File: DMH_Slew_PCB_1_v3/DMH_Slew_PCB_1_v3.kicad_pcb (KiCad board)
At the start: 2 copper layers, 48 x 175 mm, 147 parts, among them J0 Conn_01x01, J1 TS_Jack_6.35mm_Sw, J10 TS_Jack_6.35mm_Sw, J100 IDC_02x08, J2 TS_Jack_6.35mm_Sw, J200 IDC_02x05, J3 TS_Jack_6.35mm_Sw, J4 TS_Jack_6.35mm_Sw, J5 TS_Jack_6.35mm_Sw, J50 Conn_01x08_PinHeader, J51 Conn_01x08_PinHeader, J6 TS_Jack_6.35mm_Sw, J60 Conn_01x08_PinHeader, J61 Conn_01x08_PinHeader, J7 TS_Jack_6.35mm_Sw, J8 TS_Jack_6.35mm_Sw, J9 TS_Jack_6.35mm_Sw, Q1 BC548, Q10 BC558, Q11 BC548, Q12 BC548, Q2 BC548, Q3 BC558, Q4 BC558, Q5 BC548, Q6 BC548, Q7 BC548, Q8 BC548, Q9 BC558, U1 TL074, U10 LM4040LP-10, U11 LM4040LP-10, U2 TL074, U3 TL074, U4 TL074

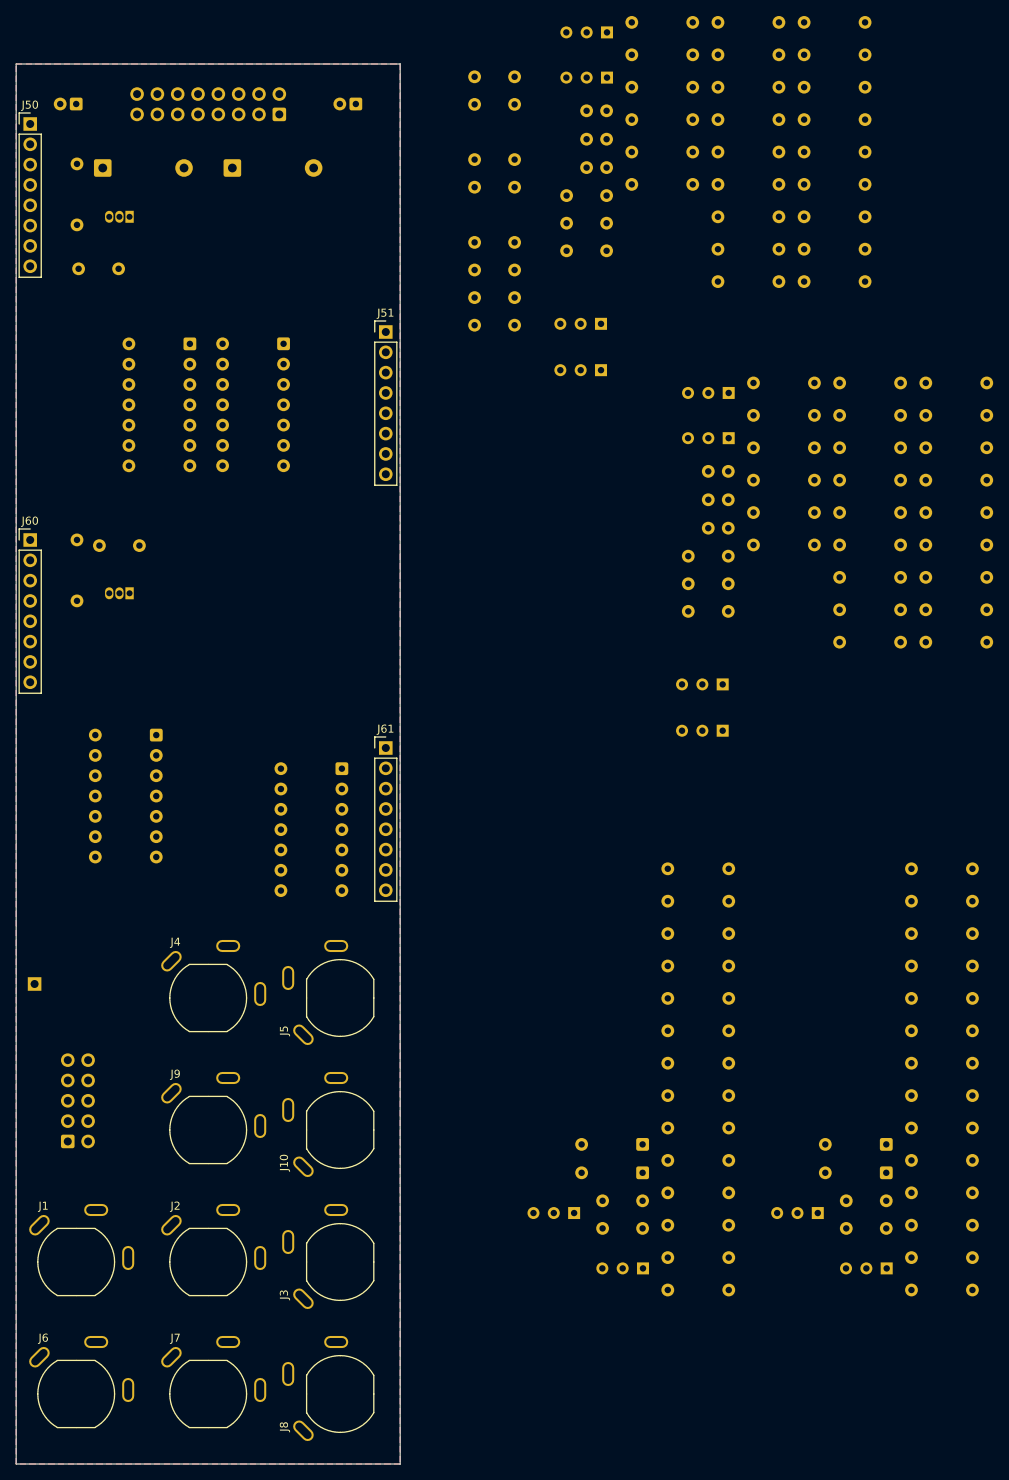
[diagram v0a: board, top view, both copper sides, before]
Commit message: Relinked PCB1 and 2 with new v3 schematics
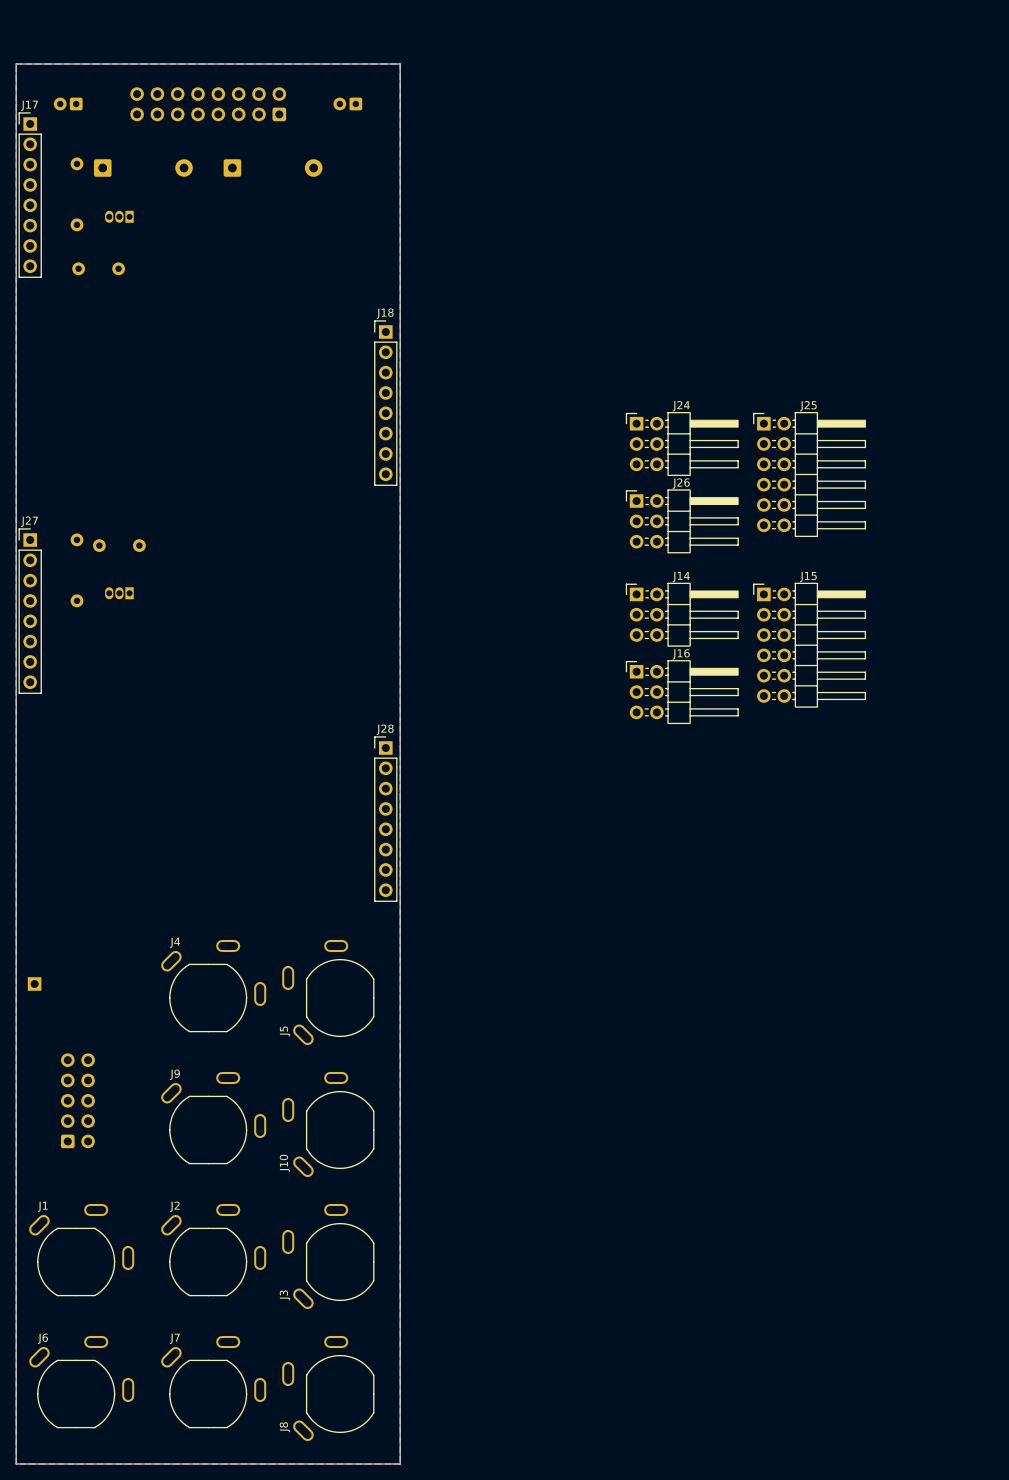
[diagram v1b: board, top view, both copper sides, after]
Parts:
- removed C10, C11, C17, C18, C19, C20, C3, C4: 100nF, Capacitor_THT:C_Disc_D4.3mm_W1.9mm_P5.00mm
- removed C12, C27: 1uF, Capacitor_THT:C_Disc_D4.3mm_W1.9mm_P5.00mm
- removed C13, C15, C22, C28: 220nF, Capacitor_THT:C_Disc_D4.3mm_W1.9mm_P5.00mm
- removed C14, C23: 22nF, Capacitor_THT:C_Disc_D4.3mm_W1.9mm_P5.00mm
- removed C21, C25, C26, C6, C7, C8: 10pF, Capacitor_THT:C_Disc_D3.0mm_W2.0mm_P2.50mm
- removed C24, C9: 2.2nF, Capacitor_THT:C_Disc_D4.3mm_W1.9mm_P5.00mm
- removed D1, D2, D7, D8: 1N4148, Diode_THT:D_DO-35_SOD27_P7.62mm_Horizontal
- removed Q1, Q11, Q12, Q2, Q5, Q6, Q7, Q8: BC548, Package_TO_SOT_THT:TO-92L_Inline_Wide
- removed Q10, Q3, Q4, Q9: BC558, Package_TO_SOT_THT:TO-92L_Inline_Wide
- removed R1, R14, R26, R35, R36, R52, R69, R70, R80, R86: 1k, Resistor_THT:R_Axial_DIN0207_L6.3mm_D2.5mm_P7.62mm_Horizontal
- removed R10, R11, R12, R13, R16, R2, R22, R23, R33, R34, R47, R48, R5, R50, R51, R53, R54, R57, R59, R6, R60, R64, R65, R7, R71, R72, R8, R82, R9, R90: 100k, Resistor_THT:R_Axial_DIN0207_L6.3mm_D2.5mm_P7.62mm_Horizontal
- removed R15, R24, R25, R63, R66, R73: 220k, Resistor_THT:R_Axial_DIN0207_L6.3mm_D2.5mm_P7.62mm_Horizontal
- removed R17, R28, R29, R30, R39, R40, R74, R77, R81, R84, R85, R88: 10k, Resistor_THT:R_Axial_DIN0207_L6.3mm_D2.5mm_P7.62mm_Horizontal
- removed R18, R19, R20, R21, R37, R67, R68, R75, R76, R78: 1k8, Resistor_THT:R_Axial_DIN0207_L6.3mm_D2.5mm_P7.62mm_Horizontal
- removed R27, R83: 100R, Resistor_THT:R_Axial_DIN0207_L6.3mm_D2.5mm_P7.62mm_Horizontal
- removed R31, R32, R79, R89: 4M7, Resistor_THT:R_Axial_DIN0207_L6.3mm_D2.5mm_P7.62mm_Horizontal
- removed R38, R87: 2k2, Resistor_THT:R_Axial_DIN0207_L6.3mm_D2.5mm_P7.62mm_Horizontal
- removed U1, U2, U3, U4: TL074, Package_DIP:DIP-14_W7.62mm_Socket
- added J14: Conn_02x03_Top_Bottom, Connector_PinHeader_2.54mm:PinHeader_2x03_P2.54mm_Horizontal, F.Cu at (128.6, 108.8)
- added J15: Conn_02x06_Top_Bottom, Connector_PinHeader_2.54mm:PinHeader_2x06_P2.54mm_Horizontal, F.Cu at (144.5, 108.8)
- added J16: Conn_02x03_Top_Bottom, Connector_PinHeader_2.54mm:PinHeader_2x03_P2.54mm_Horizontal, F.Cu at (128.6, 118.5)
- added J24: Conn_02x03_Top_Bottom, Connector_PinHeader_2.54mm:PinHeader_2x03_P2.54mm_Horizontal, F.Cu at (128.6, 87.5)
- added J25: Conn_02x06_Top_Bottom, Connector_PinHeader_2.54mm:PinHeader_2x06_P2.54mm_Horizontal, F.Cu at (144.5, 87.5)
- added J26: Conn_02x03_Top_Bottom, Connector_PinHeader_2.54mm:PinHeader_2x03_P2.54mm_Horizontal, F.Cu at (128.6, 97.1)
- J17: renamed from J50; value Conn_01x08_PinHeader -> Conn_01x08
- J18: renamed from J51; value Conn_01x08_PinHeader -> Conn_01x08
- J27: renamed from J60; value Conn_01x08_PinHeader -> Conn_01x08
- J28: renamed from J61; value Conn_01x08_PinHeader -> Conn_01x08
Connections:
- net /Core Circuit A/Bus CV renamed Bus_CV_M
- net /Core Circuit A/Output renamed A_Out_Jack_M
- net /Core Circuit B/Output renamed B_Out_Jack_M
- net F Gate A TN renamed A_F_Gate_Jack_TN_M
- net F Gate B TN renamed B_F_Gate_Jack_TN_M
- net In B TN renamed B_Input_Jack_TN_M
- net Out A TN renamed A_Out_Jack_TN_M
- net Out B TN renamed B_Out_Jack_TN_M
- net R Gate A TN renamed A_R_Gate_Jack_TN_M
- net R Gate B TN renamed B_R_Gate_Jack_TN_M
- J1 pad T: /Core Circuit A/Input -> A_Input_Jack_M
- J10 pad T: Net-(J10-PadT) -> B_F_Gate_Jack_M
- J17 pad 2: Net-(J50B-Pin_2) -> A_Diff_Amp_M
- J17 pad 3: /Core Circuit A/Rise_CV -> A_Rise_CV_M
- J17 pad 4: /Core Circuit A/Fall_CV -> A_Fall_CV_M
- J17 pad 6: Net-(J50F-Pin_6) -> A_CV_Buff_M
- J18 pad 1: Net-(J51A-Pin_1) -> A_LinLog_Sw_p5_M
- J18 pad 2: Net-(J51B-Pin_2) -> A_LinLog_Sw_p2_M
- J18 pad 3: Net-(J51C-Pin_3) -> A_R_LED_M
- J18 pad 4: Net-(J51D-Pin_4) -> A_F_LED_M
- J18 pad 5: Net-(J51E-Pin_5) -> A_Rng_Sw_p3_M
- J18 pad 7: Net-(J51G-Pin_7) -> A_Rng_Sw_p1_M
- J2 pad T: Net-(J2-PadT) -> A_CV_In_Jack_M
- J27 pad 2: Net-(J60B-Pin_2) -> B_Diff_Amp_M
- J27 pad 3: /Core Circuit B/Rise_CV -> B_Rise_CV_M
- J27 pad 4: /Core Circuit B/Fall_CV -> B_Fall_CV_M
- J27 pad 6: Net-(J60F-Pin_6) -> B_CV_Buff_M
- J28 pad 1: Net-(J61A-Pin_1) -> B_LinLog_Sw_p5_M
- J28 pad 2: Net-(J61B-Pin_2) -> B_LinLog_Sw_p2_M
- J28 pad 3: Net-(J61C-Pin_3) -> B_R_LED_M
- J28 pad 4: Net-(J61D-Pin_4) -> B_F_LED_M
- J28 pad 5: Net-(J61E-Pin_5) -> B_Rng_Sw_p3_M
- J28 pad 7: Net-(J61G-Pin_7) -> B_Rng_Sw_p1_M
- J4 pad T: Net-(J4-PadT) -> A_R_Gate_Jack_M
- J5 pad T: Net-(J5-PadT) -> A_F_Gate_Jack_M
- J6 pad T: /Core Circuit B/Input -> B_Input_Jack_M
- J7 pad T: Net-(J7-PadT) -> B_CV_In_Jack_M
- J9 pad T: Net-(J9-PadT) -> B_R_Gate_Jack_M

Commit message: PCB 1 component placement done
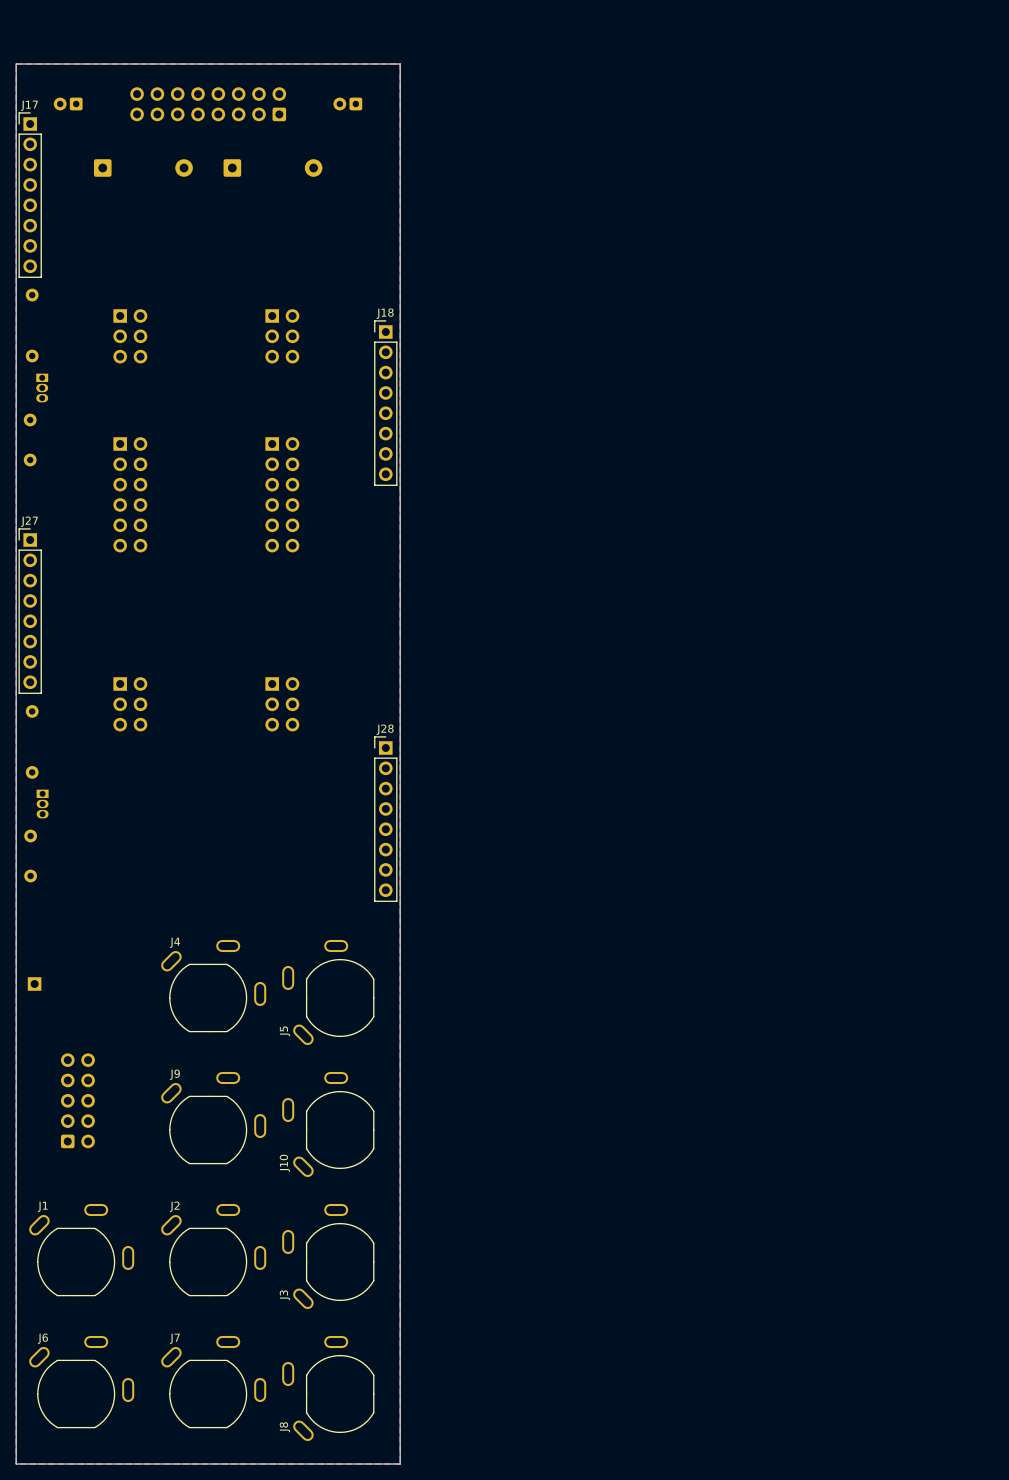
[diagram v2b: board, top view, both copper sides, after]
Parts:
- J14, J16, J24, J26: footprint Connector_PinHeader_2.54mm:PinHeader_2x03_P2.54mm_Horizontal -> Connector_PinSocket_2.54mm:PinSocket_2x03_P2.54mm_Vertical; moved to B.Cu
- J15, J25: footprint Connector_PinHeader_2.54mm:PinHeader_2x06_P2.54mm_Horizontal -> Connector_PinSocket_2.54mm:PinSocket_2x06_P2.54mm_Vertical; moved to B.Cu
- moved J15 82.6 mm to (64.0, 90.0), turned to 180 degrees
- moved J14 73.3 mm to (64.0, 74.0), turned to 180 degrees
- moved J16 64.6 mm to (64.0, 120.0), turned to 180 degrees
- moved J25 61.5 mm to (83.0, 90.0), turned to 180 degrees
- moved J26 51.0 mm to (83.0, 120.0), turned to 180 degrees
- moved J24 47.5 mm to (83.0, 74.0), turned to 180 degrees
- moved C16 38.8 mm to (52.8, 139.0), turned to -90 degrees
- moved U11 27.3 mm to (54.3, 133.7), turned to -90 degrees
- moved U10 22.9 mm to (54.2, 81.7), turned to -90 degrees
- moved R45 22.2 mm to (53.0, 131.1)
- moved C5 21.9 mm to (52.8, 87.0), turned to -90 degrees
- moved R49 17.3 mm to (53.0, 79.0)

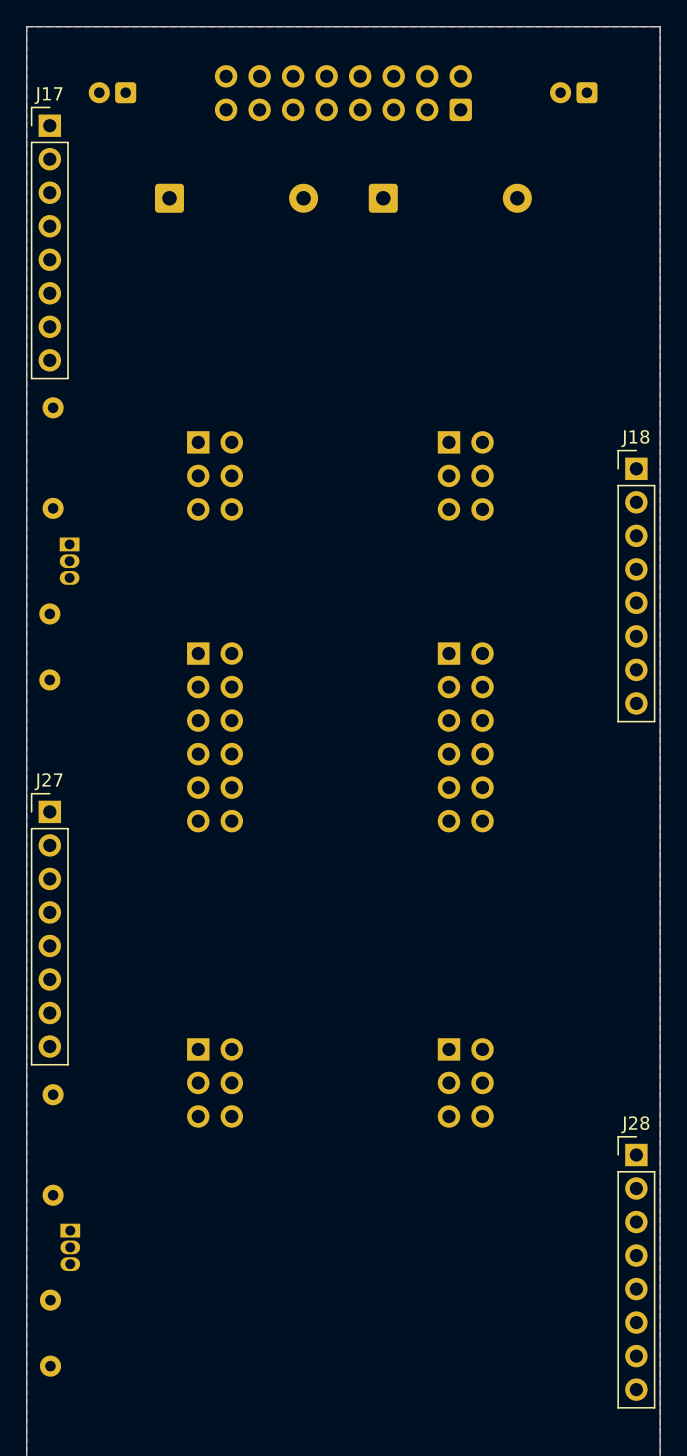
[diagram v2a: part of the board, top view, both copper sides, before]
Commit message: PCB 1 routing in progress
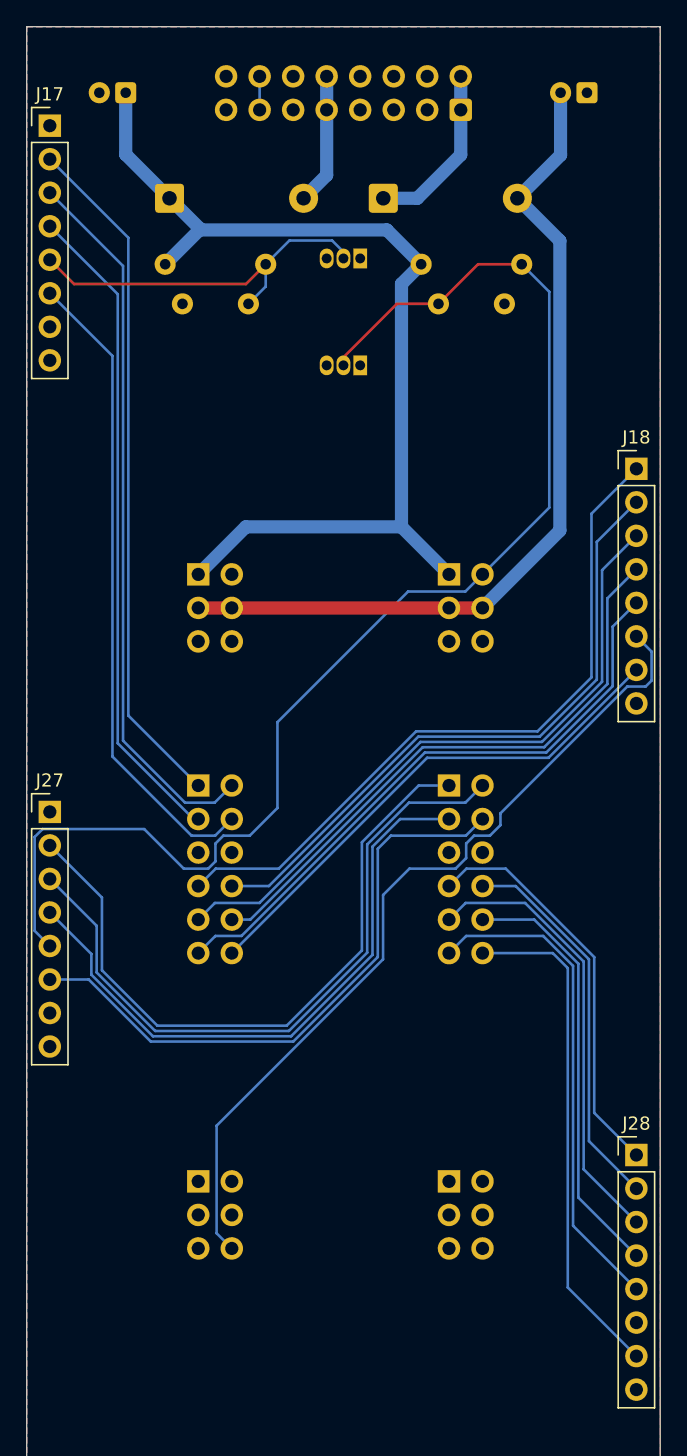
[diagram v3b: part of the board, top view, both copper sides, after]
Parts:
- moved C16 81.0 mm to (82.2, 63.5), turned to 0 degrees
- moved R45 79.0 mm to (88.5, 60.5), turned to 180 degrees
- moved U11 69.2 mm to (76.3, 68.2), turned to 180 degrees
- moved U10 30.9 mm to (76.3, 60.1), turned to 180 degrees
- moved C5 27.9 mm to (67.8, 63.5), turned to 180 degrees
- moved R49 24.5 mm to (69.1, 60.5), turned to 180 degrees
- moved J14 10.0 mm to (64.0, 84.0)
- moved J15 10.0 mm to (64.0, 100.0)
- moved J16 10.0 mm to (64.0, 130.0)
- moved J24 10.0 mm to (83.0, 84.0)
- moved J25 10.0 mm to (83.0, 100.0)
- moved J26 10.0 mm to (83.0, 130.0)
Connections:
- J14 pad 3: GND -> -12V
- J24 pad 3: GND -> -12V
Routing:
- net +10V_B: track 0.00 -> 101.5 mm
- net +12V: track 0.00 -> 76.8 mm
- net -12V: track 0.00 -> 65.7 mm
- net A_Out_Jack_M: track 0.00 -> 64.6 mm
- net A_Rise_CV_M: track 0.00 -> 54.5 mm
- net A_LinLog_Sw_p5_M: track 0.00 -> 53.6 mm
- net B_Rise_CV_M: track 0.00 -> 52.1 mm
- net A_Diff_Amp_M: track 0.00 -> 52.1 mm
- net B_Diff_Amp_M: track 0.00 -> 51.5 mm
- net A_R_LED_M: track 0.00 -> 50.2 mm
- net A_Fall_CV_M: track 0.00 -> 49.8 mm
- net A_CV_Buff_M: track 0.00 -> 49.1 mm
- net A_LinLog_Sw_p2_M: track 0.00 -> 48.8 mm
- net A_Rng_Sw_p3_M: track 0.00 -> 46.8 mm
- net B_Fall_CV_M: track 0.00 -> 46.7 mm
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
